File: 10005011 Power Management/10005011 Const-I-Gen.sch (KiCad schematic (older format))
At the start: 0 parts

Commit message: Merge branch powermanagement-dev_DotMatrix2
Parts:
- added C11, C20, C51, C66, C67, C73: 10uF, symbol Device:C
- added C21, C80, C90: 4.7uF, symbol Device:C
- added C68: 56pF, symbol Device:C
- added C69, C70, C71, C75, C78, C79: 100nF, symbol Device:C
- added C72: 33nF, symbol Device:C
- added C74: 1nF, symbol Device:C
- added C76: 330nF, symbol Device:C
- added C77, C81: 100pF, symbol Device:C
- added C83: 10nF, symbol Device:C
- added C84: 1uF, symbol Device:C
- added D8, D9: PMEG4005ET, Package_TO_SOT_SMD:SOT-23, symbol pages4_5:PMEGxx05ET
- added IC?: LT1620CMS8, symbol 10005011_Power_Management:LT1620CMS8
- added IC?: LTC1435CS, Package_SO:SOIC-16_3.9x9.9mm_P1.27mm, symbol pages4_5:LTC1435CS
- added L12: 47uH, symbol Device:L_Core_Iron
- added R126, R88: 390_2616, 10005011 Power Management:R_TE_SMF390RJT, symbol 10005011_Power_Management_Schematic_Symbols:390_2616
- added R79: 1.5M, Resistor_SMD:R_0603_1608Metric, symbol 10005011_Power_Management_Schematic_Symbols:1.5M
- added R80: 0.05_2010, Resistor_SMD:R_2010_5025Metric, symbol 10005011_Power_Management_Schematic_Symbols:0.05_2010
- added R81: 13.7k, Resistor_SMD:R_0603_1608Metric, symbol 10005011_Power_Management_Schematic_Symbols:13.7k
- added R82, R93: 1k, Resistor_SMD:R_0603_1608Metric, symbol 10005011_Power_Management_Schematic_Symbols:1k
- added R83, R84, R86, R89: 10k, Resistor_SMD:R_0603_1608Metric, symbol 10005011_Power_Management_Schematic_Symbols:10k
- added R85: 2.87k, Resistor_SMD:R_0603_1608Metric, symbol 10005011_Power_Management_Schematic_Symbols:2.87k
- added R87: 86.6k, Resistor_SMD:R_0603_1608Metric, symbol 10005011_Power_Management_Schematic_Symbols:86.6k
- added R90: 1.37k, Resistor_SMD:R_0603_1608Metric, symbol 10005011_Power_Management_Schematic_Symbols:1.37k
- added R91: 16.2k, Resistor_SMD:R_0603_1608Metric, symbol 10005011_Power_Management_Schematic_Symbols:16.2k
- added R92: 3.3k, Resistor_SMD:R_0603_1608Metric, symbol 10005011_Power_Management_Schematic_Symbols:3.3k
- added R94 (x2), R96: 100k, Resistor_SMD:R_0603_1608Metric, symbol 10005011_Power_Management_Schematic_Symbols:100k
- added R95: 33, Resistor_SMD:R_0603_1608Metric, symbol 10005011_Power_Management_Schematic_Symbols:33
- added T24, T27: IRFR024NTRPBF, Package_TO_SOT_SMD:TO-252-2, symbol 10005011_Power_Management_Schematic_Symbols:IRFR024NTRPBF
- added T25, T26: SUD50P06-15L, Package_TO_SOT_SMD:TO-252-2, symbol 10005011_Power_Management_Schematic_Symbols:SUD50P06-15L-E3
- added T28, T30: 2N7002, Package_TO_SOT_SMD:SOT-23, symbol 10005011_Power_Management_Schematic_Symbols:2N7002AQ
- added T29: IRLML2803, Package_TO_SOT_SMD:SOT-23, symbol 10005011_Power_Management_Schematic_Symbols:IRLML2803TRPBF
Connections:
- net labels added: +ISENSE, -ISENSE, CHARGER-SWITCH, GND, I-CHARGE, ICHARGE-SETTING, INTVCC-2, ITH, ITHTH, MES-VCHARGE, PGND, PROG-LT1620, VACDC, VCHARGE-SETTING, VOSENSE-2
- wire segments 0 -> 222
- no-connect marks 0 -> 1

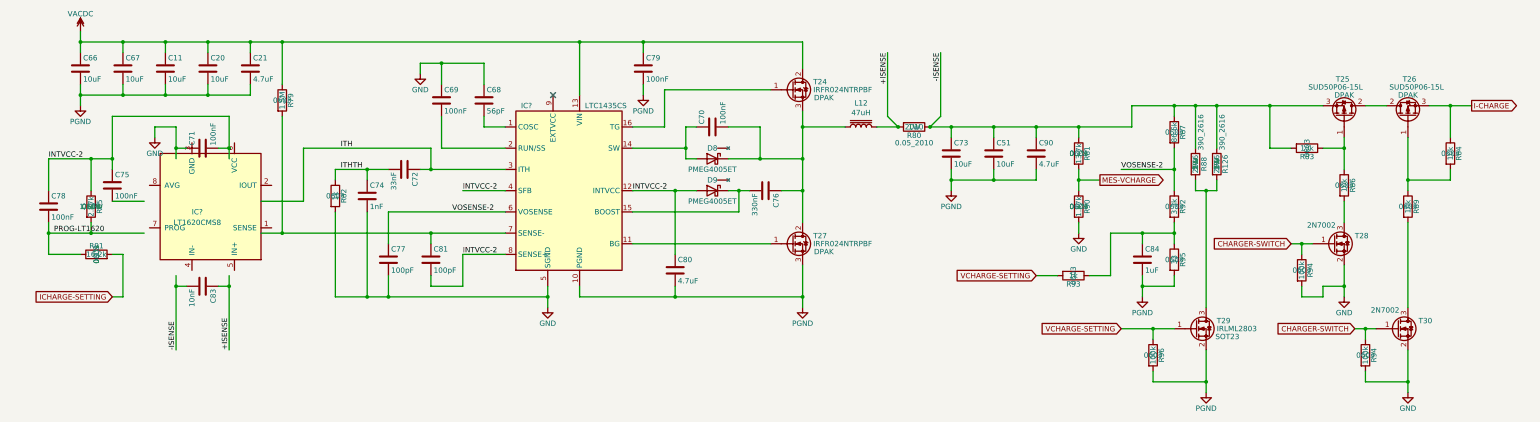
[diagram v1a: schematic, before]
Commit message: sheet5 refdes readable position
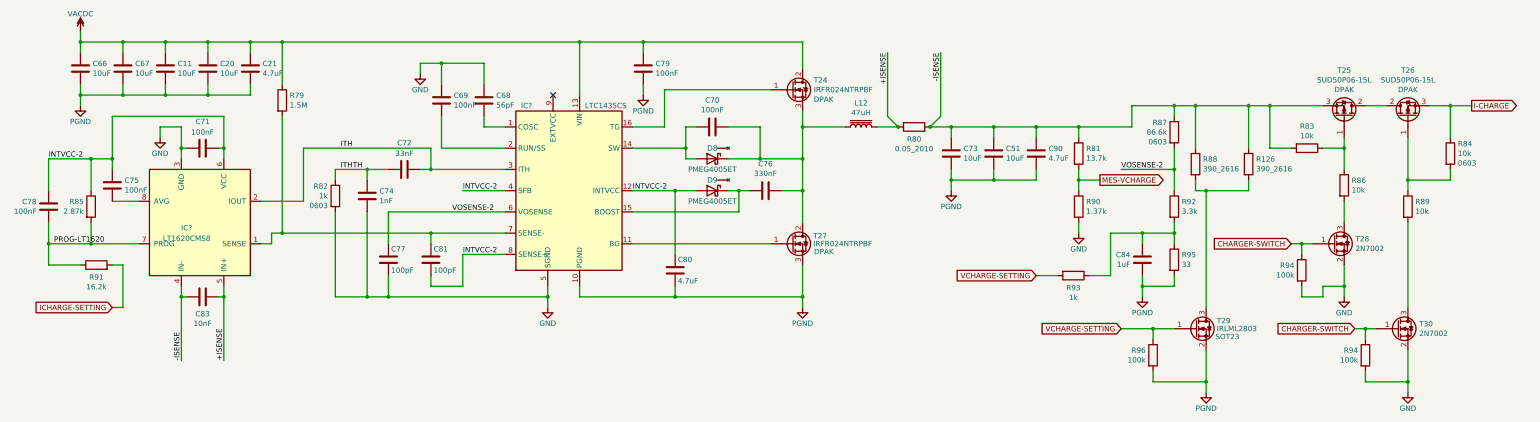
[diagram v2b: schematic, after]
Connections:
- wire segments 222 -> 224
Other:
- moved on the sheet: C83, IC?, R126, R91

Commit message: all components with refdes
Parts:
- gave numbers to parts that had none: 2
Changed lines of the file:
@@
 $EndComp
 $Comp
-L 10005011_Power_Management:LT1620CMS8 IC?
+L 10005011_Power_Management:LT1620CMS8 IC14
 U 1 1 5E97706E
 P 2350 4900
-F 0 "IC?" H 2400 4850 50  0000 C CNN
+F 0 "IC14" H 2400 4850 50  0000 C CNN
 F 1 "LT1620CMS8" H 2400 4950 50  0000 C CNN
 F 2 "" H 2450 5000 50  0001 C CNN
@@
 PROG-LT1620
 $Comp
-L pages4_5:LTC1435CS IC?
+L pages4_5:LTC1435CS IC13
 U 1 1 5E9A46CA
 P 5900 4500
-F 0 "IC?" H 5500 5300 50  0000 C CNN
+F 0 "IC13" H 5500 5300 50  0000 C CNN
 F 1 "LTC1435CS" H 6050 5300 50  0000 L CNN
 F 2 "Package_SO:SOIC-16_3.9x9.9mm_P1.27mm" V 5850 4550 50  0001 C CNN

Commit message: footprints sheet6 and small fix to sheet7
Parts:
- IC14: footprint (none) -> 10005011 Power Management:uSO08_1
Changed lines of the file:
@@
 U 1 1 5E97706E
 P 2350 4900
-F 0 "IC14" H 2400 4850 50  0000 C CNN
-F 1 "LT1620CMS8" H 2400 4950 50  0000 C CNN
-F 2 "" H 2450 5000 50  0001 C CNN
+F 0 "IC14" H 2000 5350 50  0000 R CNN
+F 1 "LT1620CMS8" H 2000 5450 50  0000 R CNN
+F 2 "10005011 Power Management:uSO08_1" H 2450 5000 50  0001 C CNN
 F 3 "https://www.analog.com/media/en/technical-documentation/data-sheets/16201f.pdf" H 2450 5000 50  0001 C CNN
 F 4 "IC,CURRENT AMPLIFIER,MSOP" H 2450 5000 50  0001 C CNN "Description"

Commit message: updating footprints
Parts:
- R79, R81, R82, R83, R84, R85, R86, R87, R89, R90, R91, R92, R93, R94, R95, R96: footprint Resistor_SMD:R_0603_1608Metric -> 10005011 Power Management:R0603_1
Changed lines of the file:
@@
 F 0 "R79" H 3270 3696 50  0000 L CNN
 F 1 "1.5M" H 3270 3605 50  0000 L CNN
-F 2 "Resistor_SMD:R_0603_1608Metric" V 3130 3650 50  0001 C CNN
+F 2 "10005011 Power Management:R0603_1" V 3130 3650 50  0001 C CNN
 F 3 "https://www.yageo.com/upload/media/product/productsearch/datasheet/rchip/PYu-RC_Group_51_RoHS_L_10.pdf" H 3200 3650 50  0001 C CNN
 F 4 "Yageo" H 3200 3650 50  0001 C CNN "Mfgr"
@@
 F 0 "R91" V 1335 5200 50  0000 C CNN
 F 1 "16.2k" V 1244 5200 50  0000 C CNN
-F 2 "Resistor_SMD:R_0603_1608Metric" V 1380 5200 50  0001 C CNN
+F 2 "10005011 Power Management:R0603_1" V 1380 5200 50  0001 C CNN
 F 3 "https://industrial.panasonic.com/cdbs/www-data/pdf/RDM0000/AOA0000C307.pdf" H 1450 5200 50  0001 C CNN
 F 4 "Panasonic Electronic Components" H 1450 5200 50  0001 C CNN "Mfgr"
@@
 F 0 "R85" H 1331 4696 50  0000 R CNN
 F 1 "2.87k" H 1331 4605 50  0000 R CNN
-F 2 "Resistor_SMD:R_0603_1608Metric" V 1330 4650 50  0001 C CNN
+F 2 "10005011 Power Management:R0603_1" V 1330 4650 50  0001 C CNN
 F 3 "https://www.mouser.com/datasheet/2/414/PCF-1528243.pdf" H 1400 4650 50  0001 C CNN
 F 4 "IRC / TT Electronics" H 1400 4650 50  0001 C CNN "Mfgr"
@@
 F 0 "R82" H 3630 4641 50  0000 R CNN
 F 1 "1k" H 3630 4550 50  0000 R CNN
-F 2 "Resistor_SMD:R_0603_1608Metric" V 3630 4550 50  0001 C CNN
+F 2 "10005011 Power Management:R0603_1" V 3630 4550 50  0001 C CNN
 F 3 "https://www.bourns.com/docs/Product-Datasheets/CHPREZTR.pdf" H 3700 4550 50  0001 C CNN
 F 4 "Bourns Inc." H 3700 4550 50  0001 C CNN "Mfgr"
@@
 F 0 "R81" H 10770 4196 50  0000 L CNN
 F 1 "13.7k" H 10770 4105 50  0000 L CNN
-F 2 "Resistor_SMD:R_0603_1608Metric" V 10630 4150 50  0001 C CNN
+F 2 "10005011 Power Management:R0603_1" V 10630 4150 50  0001 C CNN
 F 3 "https://industrial.panasonic.com/cdbs/www-data/pdf/RDM0000/AOA0000C307.pdf" H 10700 4150 50  0001 C CNN
 F 4 "Panasonic Electronic Components" H 10700 4150 50  0001 C CNN "Mfgr"
@@
 F 0 "R90" H 10770 4696 50  0000 L CNN
 F 1 "1.37k" H 10770 4605 50  0000 L CNN
-F 2 "Resistor_SMD:R_0603_1608Metric" V 10630 4650 50  0001 C CNN
+F 2 "10005011 Power Management:R0603_1" V 10630 4650 50  0001 C CNN
 F 3 "https://industrial.panasonic.com/cdbs/www-data/pdf/RDM0000/AOA0000C307.pdf" H 10700 4650 50  0001 C CNN
 F 4 "Panasonic Electronic Components" H 10700 4650 50  0001 C CNN "Mfgr"
@@
 F 0 "R87" H 11531 4041 50  0000 R CNN
 F 1 "86.6k" H 11531 3950 50  0000 R CNN
-F 2 "Resistor_SMD:R_0603_1608Metric" V 11530 3950 50  0001 C CNN
+F 2 "10005011 Power Management:R0603_1" V 11530 3950 50  0001 C CNN
 F 3 "https://industrial.panasonic.com/cdbs/www-data/pdf/RDA0000/AOA0000C304.pdf" H 11600 3950 50  0001 C CNN
 F 4 "Panasonic Electronic Components" H 11600 3950 50  0001 C CNN "Mfgr"
@@
 F 0 "R92" H 11670 4696 50  0000 L CNN
 F 1 "3.3k" H 11670 4605 50  0000 L CNN
-F 2 "Resistor_SMD:R_0603_1608Metric" V 11530 4650 50  0001 C CNN
+F 2 "10005011 Power Management:R0603_1" V 11530 4650 50  0001 C CNN
 F 3 "https://www.yageo.com/upload/media/product/productsearch/datasheet/rchip/PYu-RC_Group_51_RoHS_L_10.pdf" H 11600 4650 50  0001 C CNN
 F 4 "Yageo" H 11600 4650 50  0001 C CNN "Mfgr"
@@
 F 0 "R95" H 11670 5196 50  0000 L CNN
 F 1 "33" H 11670 5105 50  0000 L CNN
-F 2 "Resistor_SMD:R_0603_1608Metric" V 11530 5150 50  0001 C CNN
+F 2 "10005011 Power Management:R0603_1" V 11530 5150 50  0001 C CNN
 F 3 "https://www.yageo.com/upload/media/product/productsearch/datasheet/rchip/PYu-RC_Group_51_RoHS_L_10.pdf" H 11600 5150 50  0001 C CNN
 F 4 "Yageo" H 11600 5150 50  0001 C CNN "Mfgr"
@@
 F 0 "R93" V 10765 5300 50  0000 C CNN
 F 1 "1k" V 10856 5300 50  0000 C CNN
-F 2 "Resistor_SMD:R_0603_1608Metric" V 10580 5300 50  0001 C CNN
+F 2 "10005011 Power Management:R0603_1" V 10580 5300 50  0001 C CNN
 F 3 "https://www.bourns.com/docs/Product-Datasheets/CHPREZTR.pdf" H 10650 5300 50  0001 C CNN
 F 4 "Bourns Inc." H 10650 5300 50  0001 C CNN "Mfgr"
@@
 F 0 "R96" H 11331 6096 50  0000 R CNN
 F 1 "100k" H 11331 6005 50  0000 R CNN
-F 2 "Resistor_SMD:R_0603_1608Metric" V 11330 6050 50  0001 C CNN
+F 2 "10005011 Power Management:R0603_1" V 11330 6050 50  0001 C CNN
 F 3 "https://www.yageo.com/upload/media/product/productsearch/datasheet/rchip/PYu-RC_Group_51_RoHS_L_10.pdf" H 11400 6050 50  0001 C CNN
 F 4 "Yageo" H 11400 6050 50  0001 C CNN "Mfgr"
@@
 F 0 "R83" V 12643 4100 50  0000 C CNN
 F 1 "10k" V 12734 4100 50  0000 C CNN
-F 2 "Resistor_SMD:R_0603_1608Metric" V 12780 4100 50  0001 C CNN
+F 2 "10005011 Power Management:R0603_1" V 12780 4100 50  0001 C CNN
 F 3 "https://www.yageo.com/upload/media/product/productsearch/datasheet/rchip/PYu-RC_Group_51_RoHS_L_10.pdf" H 12850 4100 50  0001 C CNN
 F 4 "Yageo" H 12850 4100 50  0001 C CNN "Mfgr"
@@
 F 0 "R86" H 13270 4496 50  0000 L CNN
 F 1 "10k" H 13270 4405 50  0000 L CNN
-F 2 "Resistor_SMD:R_0603_1608Metric" V 13130 4450 50  0001 C CNN
+F 2 "10005011 Power Management:R0603_1" V 13130 4450 50  0001 C CNN
 F 3 "https://www.yageo.com/upload/media/product/productsearch/datasheet/rchip/PYu-RC_Group_51_RoHS_L_10.pdf" H 13200 4450 50  0001 C CNN
 F 4 "Yageo" H 13200 4450 50  0001 C CNN "Mfgr"
@@
 F 0 "R94" H 12731 5296 50  0000 R CNN
 F 1 "100k" H 12731 5205 50  0000 R CNN
-F 2 "Resistor_SMD:R_0603_1608Metric" V 12730 5250 50  0001 C CNN
+F 2 "10005011 Power Management:R0603_1" V 12730 5250 50  0001 C CNN
 F 3 "https://www.yageo.com/upload/media/product/productsearch/datasheet/rchip/PYu-RC_Group_51_RoHS_L_10.pdf" H 12800 5250 50  0001 C CNN
 F 4 "Yageo" H 12800 5250 50  0001 C CNN "Mfgr"
@@
 F 0 "R94" H 13331 6096 50  0000 R CNN
 F 1 "100k" H 13331 6005 50  0000 R CNN
-F 2 "Resistor_SMD:R_0603_1608Metric" V 13330 6050 50  0001 C CNN
+F 2 "10005011 Power Management:R0603_1" V 13330 6050 50  0001 C CNN
 F 3 "https://www.yageo.com/upload/media/product/productsearch/datasheet/rchip/PYu-RC_Group_51_RoHS_L_10.pdf" H 13400 6050 50  0001 C CNN
 F 4 "Yageo" H 13400 6050 50  0001 C CNN "Mfgr"
@@
 F 0 "R89" H 13870 4696 50  0000 L CNN
 F 1 "10k" H 13870 4605 50  0000 L CNN
-F 2 "Resistor_SMD:R_0603_1608Metric" V 13730 4650 50  0001 C CNN
+F 2 "10005011 Power Management:R0603_1" V 13730 4650 50  0001 C CNN
 F 3 "https://www.yageo.com/upload/media/product/productsearch/datasheet/rchip/PYu-RC_Group_51_RoHS_L_10.pdf" H 13800 4650 50  0001 C CNN
 F 4 "Yageo" H 13800 4650 50  0001 C CNN "Mfgr"
@@
 F 0 "R84" H 14270 4241 50  0000 L CNN
 F 1 "10k" H 14270 4150 50  0000 L CNN
-F 2 "Resistor_SMD:R_0603_1608Metric" V 14130 4150 50  0001 C CNN
+F 2 "10005011 Power Management:R0603_1" V 14130 4150 50  0001 C CNN
 F 3 "https://www.yageo.com/upload/media/product/productsearch/datasheet/rchip/PYu-RC_Group_51_RoHS_L_10.pdf" H 14200 4150 50  0001 C CNN
 F 4 "Yageo" H 14200 4150 50  0001 C CNN "Mfgr"

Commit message: assigned footprints with cmp file
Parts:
- C11, C20, C51, C66, C67, C73: footprint (none) -> 10005011 Power Management:C2220_1
- C21, C90: footprint (none) -> 10005011 Power Management:C1210_1
- C68, C72, C74, C83, C84: footprint (none) -> 10005011 Power Management:C0603_1
- C69, C71, C75, C77, C78, C81: footprint (none) -> 10005011 Power Management:C0402_1
- C70, C76, C79, C80: footprint (none) -> 10005011 Power Management:C0805_1
- D8, D9: footprint Package_TO_SOT_SMD:SOT-23 -> 10005011 Power Management:SOT23-1G_1
- IC13: footprint Package_SO:SOIC-16_3.9x9.9mm_P1.27mm -> 10005011 Power Management:SSOP16_1
- L12: footprint (none) -> 10005011 Power Management:WEPD-XXL_1
- R126, R88: footprint 10005011 Power Management:R_TE_SMF390RJT -> 10005011 Power Management:SM2_1
- R80: footprint Resistor_SMD:R_2010_5025Metric -> 10005011 Power Management:R2010_1
- T24, T25, T26, T27: footprint Package_TO_SOT_SMD:TO-252-2 -> 10005011 Power Management:DPAK-GDS_1
- T28, T29, T30: footprint Package_TO_SOT_SMD:SOT-23 -> 10005011 Power Management:SOT23-GSD_1

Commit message: more footprints
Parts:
- T29: Bom_Footprint SOT23 -> (none)
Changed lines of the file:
@@
 F 7 "IRLML2803PBFCT-ND" H 12500 5725 50  0001 C CNN "Source_PN"
 F 8 "MOSFET N-CH 30V 1.2A SOT-23" H 12600 5725 50  0001 C CNN "Description"
-F 9 "SOT23" H 12100 5725 50  0000 C CNN "Bom_Footprint"
 	1    11900 5800
 	1    0    0    -1
